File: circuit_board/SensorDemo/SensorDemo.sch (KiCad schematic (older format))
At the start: 58 parts, among them K1 PB, P1 CONN3X2, P2 CONN3X2, U1 TLV1117-33CDCYR, U2 dsPIC33EP32GP502, U3 LTC1658, U4 INA126, U5 REF1925, U6 REF1925, X1 8MHz

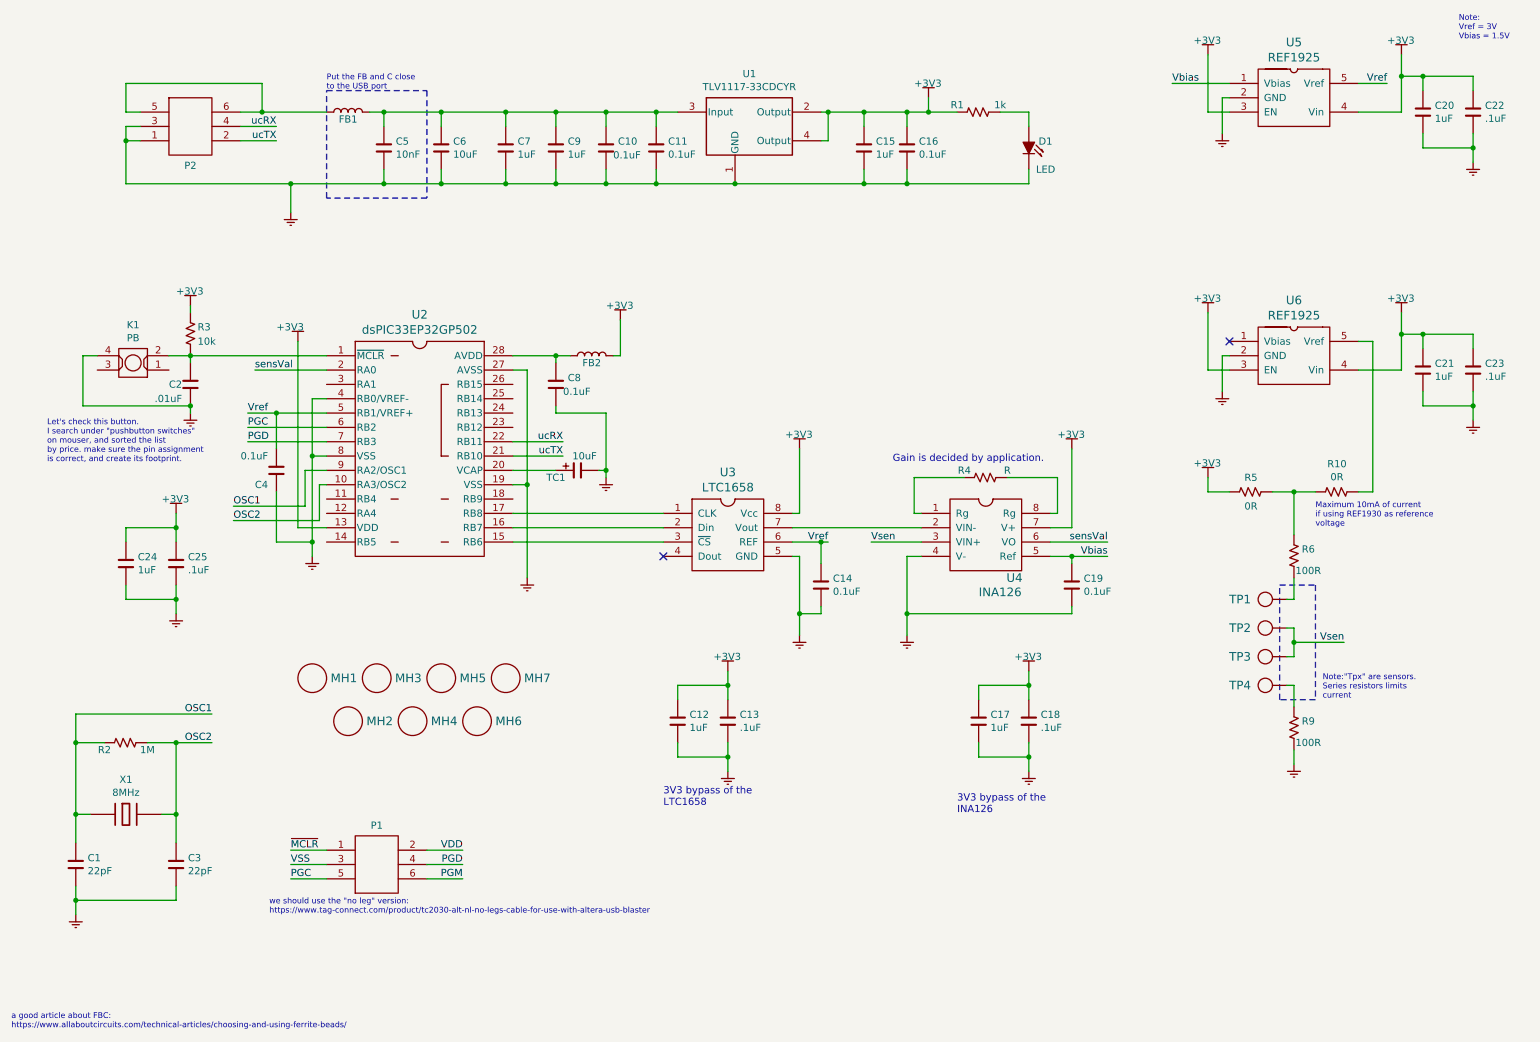
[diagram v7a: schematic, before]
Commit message: SensorDemo board updated
re-positioned all components and routed pcb.
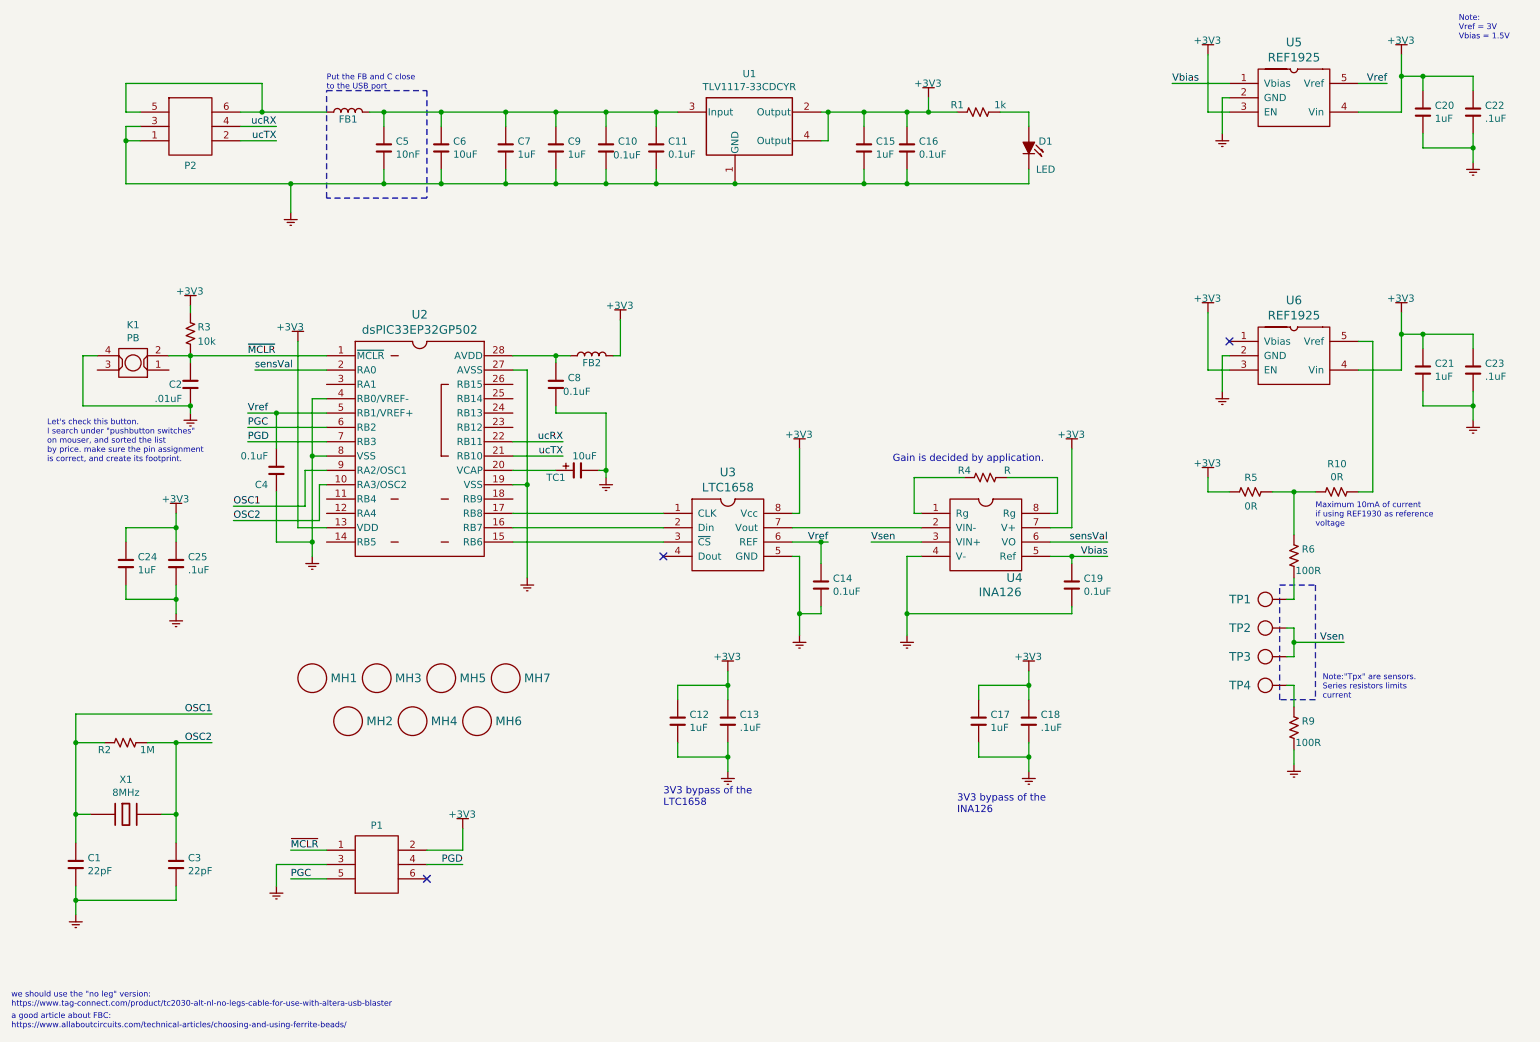
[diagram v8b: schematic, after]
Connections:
- net ~MCLR: now also C2.1, K1.2, R3.2, U2.1 (~MCLR)
- net PGM: no longer names the net of P1.6
- net VDD: no longer names the net of P1.2
- net VSS: no longer names the net of P1.3
- no-connect marks 2 -> 3
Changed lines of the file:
@@
 Text Notes 800  3800 0    40   ~ 0
 Let's check this button. \nI search under "pushbutton switches"\non mouser, and sorted the list\nby price. make sure the pin assignment\nis correct, and create its footprint.
-Text Label 3700 6700 2    50   ~ 0
-PGM
 Text Label 2500 6700 0    50   ~ 0
 PGC
 Text Label 3700 6600 2    50   ~ 0
 PGD
-Text Label 2500 6600 0    50   ~ 0
-VSS
-Text Label 3700 6500 2    50   ~ 0
-VDD
 Text Label 2500 6500 0    50   ~ 0
 ~MCLR
 Wire Wire Line
-	3700 6700 3450 6700
-Wire Wire Line
 	3700 6600 3450 6600
 Wire Wire Line
@@
 Wire Wire Line
 	2500 6700 2750 6700
-Wire Wire Line
-	2500 6600 2750 6600
 Wire Wire Line
 	2500 6500 2750 6500
@@
 Wire Wire Line
 	10050 4000 9950 4000
-Text Notes 2350 6950 0    40   ~ 0
+Text Notes 550  7600 0    40   ~ 0
 we should use the "no leg" version:\nhttps://www.tag-connect.com/product/tc2030-alt-nl-no-legs-cable-for-use-with-altera-usb-blaster
 $Comp
@@
 Wire Wire Line
 	2300 1350 2750 1350
+Text Label 2200 3050 0    50   ~ 0
+~MCLR
+NoConn ~ 3450 6700
+$Comp
+L SensorDemo_power_supply:GND #PS?
+U 1 1 6063F2B2
+P 2400 6800
+F 0 "#PS?" H 2400 6675 50  0001 C CNN
+F 1 "GND" H 2400 6725 50  0001 C CNN
+F 2 "" H 2400 6800 50  0001 C CNN
+F 3 "" H 2400 6800 50  0001 C CNN
+	1    2400 6800
+	1    0    0    -1
+$EndComp
+Wire Wire Line
+	2400 6600 2400 6750
+Wire Wire Line
+	2400 6600 2750 6600
+$Comp
+L SensorDemo_power_supply:+3V3 #PS?
+U 1 1 6064F95D
+P 3700 6350
+F 0 "#PS?" H 3700 6300 50  0001 C CNN
+F 1 "+3V3" H 3600 6450 50  0000 L CNN
+F 2 "" H 3705 6045 50  0001 C CNN
+F 3 "" H 3705 6045 50  0001 C CNN
+	1    3700 6350
+	1    0    0    -1
+$EndComp
+Wire Wire Line
+	3700 6500 3700 6350
 $EndSCHEMATC
